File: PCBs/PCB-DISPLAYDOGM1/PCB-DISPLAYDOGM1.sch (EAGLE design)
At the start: 36 parts, among them IC1 MCP23017SS, IC2 74HC14D, SW1 EC12E_SW, SW2 EC12E_SW, SW2ALT EC12E_SW

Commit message: PCBS updated
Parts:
- removed C3: 10uF, SparkFun:CAP0805
- added C10, C12: 100nF, SparkFun:CAP0603-CAP
- added C2: 22uF, SparkFun:CAP0805
- added L4: ILHB0805ER121V, SparkFun:INDUCTOR0805
- C4, C7: value 100nF -> 10nF
- R13, R4, R7: value 10K -> 0R
- R5, R6, R8: value 10K -> 100K
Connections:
- new net ARD_5V: C12.1, L4.1, SERIAL.2
- net 5V: now also C10.1, C2.1, L4.2; no longer C3.1, SERIAL.2
- net GND: now also C10.2, C12.2, C2.2; no longer C3.2
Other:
- note added: "74HCT14D"
- note removed: "POWER"
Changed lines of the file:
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@@
 <part name="SERIAL" library="SparkFun" deviceset="M04X2" device=""/>
 <part name="GND5" library="SparkFun" deviceset="GND" device=""/>
-<part name="U$17" library="SparkFun" deviceset="5V" device=""/>
 <part name="U$19" library="SKAARHOJ" deviceset="3BITADDR" device=""/>
 <part name="U$23" library="SKAARHOJ" deviceset="PCA9671" device=""/>
@@
 <part name="R1" library="SparkFun" deviceset="RESISTOR" device="0603-RES" value="30R/0.1W"/>
 <part name="R3" library="SparkFun" deviceset="RESISTOR" device="0603-RES" value="30R/0.1W"/>
-<part name="C3" library="SparkFun" deviceset="CAP" device="0805" value="10uF"/>
-<part name="U$4" library="SparkFun" deviceset="5V" device=""/>
-<part name="GND3" library="SparkFun" deviceset="GND" device=""/>
 <part name="GND2" library="SparkFun" deviceset="GND" device=""/>
 <part name="SW1" library="switch-alps" deviceset="EC12E_SW" device=""/>
-<part name="C4" library="SparkFun" deviceset="CAP" device="0603-CAP" value="100nF"/>
+<part name="C4" library="SparkFun" deviceset="CAP" device="0603-CAP" value="10nF"/>
 <part name="C5" library="SparkFun" deviceset="CAP" device="0603-CAP" value="10nF"/>
 <part name="C6" library="SparkFun" deviceset="CAP" device="0603-CAP" value="10nF"/>
-<part name="R4" library="SparkFun" deviceset="RESISTOR" device="0603-RES" value="10K"/>
+<part name="R4" library="SparkFun" deviceset="RESISTOR" device="0603-RES" value="0R"/>
 <part name="U$7" library="SKAARHOJ" deviceset="GNDPAD" device="6MM" value="GNDPAD6MM"/>
 <part name="U$21" library="SKAARHOJ" deviceset="GNDPAD" device="6MM" value="GNDPAD6MM"/>
 <part name="GND6" library="SparkFun" deviceset="GND" device=""/>
 <part name="SW2" library="switch-alps" deviceset="EC12E_SW" device=""/>
-<part name="C7" library="SparkFun" deviceset="CAP" device="0603-CAP" value="100nF"/>
+<part name="C7" library="SparkFun" deviceset="CAP" device="0603-CAP" value="10nF"/>
 <part name="C8" library="SparkFun" deviceset="CAP" device="0603-CAP" value="10nF"/>
 <part name="C9" library="SparkFun" deviceset="CAP" device="0603-CAP" value="10nF"/>
-<part name="R13" library="SparkFun" deviceset="RESISTOR" device="0603-RES" value="10K"/>
+<part name="R13" library="SparkFun" deviceset="RESISTOR" device="0603-RES" value="0R"/>
 <part name="IC1" library="microchip" deviceset="MCP23017" device="SS">
 <attribute name="MPN" value="MCP23017-E/SS"/>
@@
 <part name="U$15" library="SparkFun" deviceset="5V" device=""/>
 <part name="U$16" library="SparkFun" deviceset="5V" device=""/>
-<part name="R8" library="SparkFun" deviceset="RESISTOR" device="0603-RES" value="10K"/>
+<part name="R8" library="SparkFun" deviceset="RESISTOR" device="0603-RES" value="100K"/>
 <part name="U$18" library="SparkFun" deviceset="5V" device=""/>
 <part name="GND12" library="SparkFun" deviceset="GND" device=""/>
@@
 <part name="GND4" library="supply1" deviceset="GND" device=""/>
 <part name="U$5" library="SparkFun" deviceset="5V" device=""/>
-<part name="R5" library="SparkFun" deviceset="RESISTOR" device="0603-RES" value="10K"/>
-<part name="R6" library="SparkFun" deviceset="RESISTOR" device="0603-RES" value="10K"/>
-<part name="R7" library="SparkFun" deviceset="RESISTOR" device="0603-RES" value="10K"/>
+<part name="R5" library="SparkFun" deviceset="RESISTOR" device="0603-RES" value="100K"/>
+<part name="R6" library="SparkFun" deviceset="RESISTOR" device="0603-RES" value="100K"/>
+<part name="R7" library="SparkFun" deviceset="RESISTOR" device="0603-RES" value="0R"/>
 <part name="SW2ALT" library="switch-alps" deviceset="EC12E_SW" device=""/>
+<part name="L4" library="SparkFun" deviceset="INDUCTOR" device="0805" value="ILHB0805ER121V"/>
+<part name="C2" library="SparkFun" deviceset="CAP" device="0805" value="22uF"/>
+<part name="C10" library="SparkFun" deviceset="CAP" device="0603-CAP" value="100nF"/>
+<part name="C12" library="SparkFun" deviceset="CAP" device="0603-CAP" value="100nF"/>
+<part name="U$24" library="SparkFun" deviceset="5V" device=""/>
 </parts>
 <sheets>
@@
 <text x="121.92" y="-60.96" size="3.81" layer="97">SERIAL</text>
 <text x="129.54" y="-5.08" size="3.81" layer="97">CONFIG</text>
-<text x="190.5" y="-60.96" size="3.81" layer="97">POWER</text>
 <text x="-99.06" y="-205.74" size="1.778" layer="91">ADR=Bxxx</text>
 <text x="-101.6" y="-218.44" size="3.81" layer="97">CONFIG</text>
+<text x="78.74" y="-148.336" size="1.778" layer="91">74HCT14D</text>
+<text x="78.74" y="-222.25" size="1.778" layer="91">74HCT14D</text>
+<text x="-27.686" y="-148.59" size="1.778" layer="91">74HCT14D</text>
 </plain>
 <instances>
 <instance part="SERIAL" gate="G$1" x="137.16" y="-73.66"/>
 <instance part="GND5" gate="1" x="124.46" y="-86.36"/>
-<instance part="U$17" gate="G$1" x="147.32" y="-68.58"/>
 <instance part="U$19" gate="G$1" x="134.62" y="-22.86"/>
 <instance part="U$23" gate="G$1" x="66.04" y="-43.18" rot="R180"/>
@@
 <instance part="R1" gate="G$1" x="-43.18" y="-15.24" rot="R90"/>
 <instance part="R3" gate="G$1" x="-33.02" y="-15.24" rot="R90"/>
-<instance part="C3" gate="G$1" x="195.58" y="-78.74"/>
-<instance part="U$4" gate="G$1" x="195.58" y="-71.12"/>
-<instance part="GND3" gate="1" x="195.58" y="-86.36"/>
 <instance part="GND2" gate="1" x="7.62" y="-198.12"/>
 <instance part="SW1" gate="G$1" x="60.96" y="-157.48" rot="R90"/>
@@
 <instance part="SW2ALT" gate="G$1" x="162.56" y="-127" rot="R90"/>
 <instance part="SW2ALT" gate="G$2" x="160.02" y="-142.24"/>
+<instance part="L4" gate="G$1" x="182.88" y="-68.58" rot="R90"/>
+<instance part="C2" gate="G$1" x="205.74" y="-76.2"/>
+<instance part="C10" gate="G$1" x="193.04" y="-76.2"/>
+<instance part="C12" gate="G$1" x="172.72" y="-76.2"/>
+<instance part="U$24" gate="G$1" x="205.74" y="-66.04"/>
 </instances>
 <busses>
@@
 <nets>
 <net name="5V" class="1">
-<segment>
-<pinref part="SERIAL" gate="G$1" pin="2"/>
-<pinref part="U$17" gate="G$1" pin="5V"/>
-<wire x1="144.78" y1="-68.58" x2="147.32" y2="-68.58" width="0.1524" layer="91"/>
-</segment>
 <segment>
 <pinref part="R2" gate="G$1" pin="2"/>
@@
 </segment>
 <segment>
-<pinref part="U$4" gate="G$1" pin="5V"/>
-<pinref part="C3" gate="G$1" pin="1"/>
-<wire x1="195.58" y1="-73.66" x2="195.58" y2="-71.12" width="0.1524" layer="91"/>
-</segment>
-<segment>
 <pinref part="IC1" gate="G$1" pin="VDD"/>
 <pinref part="U$13" gate="G$1" pin="5V"/>
@@
 <pinref part="U$5" gate="G$1" pin="5V"/>
 </segment>
+<segment>
+<wire x1="190.5" y1="-68.58" x2="193.04" y2="-68.58" width="0.1524" layer="91"/>
+<pinref part="C10" gate="G$1" pin="1"/>
+<wire x1="193.04" y1="-71.12" x2="193.04" y2="-68.58" width="0.1524" layer="91"/>
+<pinref part="L4" gate="G$1" pin="2"/>
+<pinref part="C2" gate="G$1" pin="1"/>
+<wire x1="205.74" y1="-71.12" x2="205.74" y2="-68.58" width="0.1524" layer="91"/>
+<wire x1="205.74" y1="-68.58" x2="193.04" y2="-68.58" width="0.1524" layer="91"/>
+<junction x="193.04" y="-68.58"/>
+<pinref part="U$24" gate="G$1" pin="5V"/>
+<wire x1="205.74" y1="-66.04" x2="205.74" y2="-68.58" width="0.1524" layer="91"/>
+<junction x="205.74" y="-68.58"/>
+</segment>
 </net>
 <net name="GND" class="1">
@@
 <pinref part="GND5" gate="1" pin="GND"/>
 <wire x1="124.46" y1="-68.58" x2="124.46" y2="-83.82" width="0.1524" layer="91"/>
+<pinref part="C12" gate="G$1" pin="2"/>
+<wire x1="172.72" y1="-83.82" x2="172.72" y2="-78.74" width="0.1524" layer="91"/>
+<pinref part="C10" gate="G$1" pin="2"/>
+<wire x1="172.72" y1="-83.82" x2="193.04" y2="-83.82" width="0.1524" layer="91"/>
+<wire x1="193.04" y1="-83.82" x2="193.04" y2="-78.74" width="0.1524" layer="91"/>
+<pinref part="C2" gate="G$1" pin="2"/>
+<wire x1="193.04" y1="-83.82" x2="205.74" y2="-83.82" width="0.1524" layer="91"/>
+<wire x1="205.74" y1="-83.82" x2="205.74" y2="-78.74" width="0.1524" layer="91"/>
+<junction x="193.04" y="-83.82"/>
+<wire x1="172.72" y1="-83.82" x2="124.46" y2="-83.82" width="0.1524" layer="91"/>
+<junction x="172.72" y="-83.82"/>
+<junction x="124.46" y="-83.82"/>
 </segment>
 <segment>
@@
 <junction x="-35.56" y="-33.02"/>
 <label x="-30.48" y="-33.02" size="1.778" layer="95"/>
-</segment>
-<segment>
-<pinref part="GND3" gate="1" pin="GND"/>
-<pinref part="C3" gate="G$1" pin="2"/>
-<wire x1="195.58" y1="-83.82" x2="195.58" y2="-81.28" width="0.1524" layer="91"/>
 </segment>
 <segment>
@@
 <wire x1="-7.62" y1="-228.6" x2="-7.62" y2="-193.04" width="0.1524" layer="91"/>
 <junction x="-7.62" y="-193.04"/>
+<junction x="-22.86" y="-271.78"/>
 </segment>
 <segment>
@@
 </segment>
 </net>
+<net name="ARD_5V" class="1">
+<segment>
+<pinref part="L4" gate="G$1" pin="1"/>
+<pinref part="C12" gate="G$1" pin="1"/>
+<wire x1="172.72" y1="-68.58" x2="175.26" y2="-68.58" width="0.1524" layer="91"/>
+<wire x1="172.72" y1="-68.58" x2="172.72" y2="-71.12" width="0.1524" layer="91"/>
+<pinref part="SERIAL" gate="G$1" pin="2"/>
+<wire x1="172.72" y1="-68.58" x2="144.78" y2="-68.58" width="0.1524" layer="91"/>
+<junction x="172.72" y="-68.58"/>
+</segment>
+</net>

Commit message: asfd
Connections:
- new net N$7: IC2E.O, IC2F.I
- new net N$8: IC2E.I, SERIAL.7
- net GND: no longer IC2E.I, IC2F.I
- net SPI_SCLK: now also IC2F.O; no longer SERIAL.7
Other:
- moved on the sheet: IC2E, IC2F
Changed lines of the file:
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@@
 <instance part="U$5" gate="G$1" x="200.66" y="-160.02"/>
 <instance part="IC2" gate="B" x="-12.7" y="-251.46"/>
-<instance part="IC2" gate="E" x="-10.16" y="-271.78"/>
-<instance part="IC2" gate="F" x="-10.16" y="-287.02"/>
+<instance part="IC2" gate="E" x="121.92" y="-101.6"/>
+<instance part="IC2" gate="F" x="144.78" y="-101.6"/>
 <instance part="R5" gate="G$1" x="30.48" y="-149.86" rot="R90"/>
 <instance part="R6" gate="G$1" x="134.62" y="-149.86" rot="R90"/>
@@
 <pinref part="IC2" gate="B" pin="I"/>
 <wire x1="-22.86" y1="-251.46" x2="-22.86" y2="-254" width="0.1524" layer="91"/>
-<pinref part="IC2" gate="E" pin="I"/>
-<wire x1="-22.86" y1="-254" x2="-22.86" y2="-271.78" width="0.1524" layer="91"/>
-<wire x1="-22.86" y1="-271.78" x2="-20.32" y2="-271.78" width="0.1524" layer="91"/>
-<wire x1="-22.86" y1="-271.78" x2="-22.86" y2="-289.56" width="0.1524" layer="91"/>
-<pinref part="IC2" gate="F" pin="I"/>
-<wire x1="-22.86" y1="-289.56" x2="-20.32" y2="-289.56" width="0.1524" layer="91"/>
-<wire x1="-20.32" y1="-289.56" x2="-20.32" y2="-287.02" width="0.1524" layer="91"/>
 <wire x1="-22.86" y1="-254" x2="-30.48" y2="-254" width="0.1524" layer="91"/>
 <wire x1="-30.48" y1="-254" x2="-30.48" y2="-228.6" width="0.1524" layer="91"/>
-<junction x="-22.86" y="-254"/>
 <wire x1="-30.48" y1="-228.6" x2="-7.62" y2="-228.6" width="0.1524" layer="91"/>
 <wire x1="-7.62" y1="-228.6" x2="-7.62" y2="-193.04" width="0.1524" layer="91"/>
 <junction x="-7.62" y="-193.04"/>
-<junction x="-22.86" y="-271.78"/>
 </segment>
 <segment>
@@
 <net name="SPI_SCLK" class="0">
 <segment>
-<pinref part="SERIAL" gate="G$1" pin="7"/>
-<wire x1="129.54" y1="-76.2" x2="119.38" y2="-76.2" width="0.1524" layer="91"/>
-<label x="119.38" y="-76.2" size="1.778" layer="95" rot="R180"/>
-</segment>
-<segment>
 <pinref part="DISP" gate="G$1" pin="D6"/>
 <wire x1="-50.8" y1="-68.58" x2="-50.8" y2="-73.66" width="0.1524" layer="91"/>
 <label x="-50.8" y="-73.66" size="1.778" layer="95" rot="R270"/>
+</segment>
+<segment>
+<pinref part="IC2" gate="F" pin="O"/>
+<wire x1="154.94" y1="-101.6" x2="160.02" y2="-101.6" width="0.1524" layer="91"/>
+<label x="160.02" y="-101.6" size="1.778" layer="95"/>
 </segment>
 </net>
@@
 </segment>
 </net>
+<net name="N$7" class="0">
+<segment>
+<pinref part="IC2" gate="E" pin="O"/>
+<pinref part="IC2" gate="F" pin="I"/>
+<wire x1="134.62" y1="-101.6" x2="132.08" y2="-101.6" width="0.1524" layer="91"/>
+</segment>
+</net>
+<net name="N$8" class="0">
+<segment>
+<pinref part="SERIAL" gate="G$1" pin="7"/>
+<wire x1="129.54" y1="-76.2" x2="109.22" y2="-76.2" width="0.1524" layer="91"/>
+<wire x1="109.22" y1="-76.2" x2="109.22" y2="-101.6" width="0.1524" layer="91"/>
+<pinref part="IC2" gate="E" pin="I"/>
+<wire x1="109.22" y1="-101.6" x2="111.76" y2="-101.6" width="0.1524" layer="91"/>
+</segment>
+</net>

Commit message: Updates
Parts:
- SERIAL: value M04X2 -> M04X2M2X4SMALLER; device SparkFun:M04X2 -> SKAARHOJ:M04X2M2X4SMALLER
- U$10, U$19: value 3BITADDR -> 3BITADDRSMALL; device SKAARHOJ:3BITADDR -> SKAARHOJ:3BITADDRSMALL

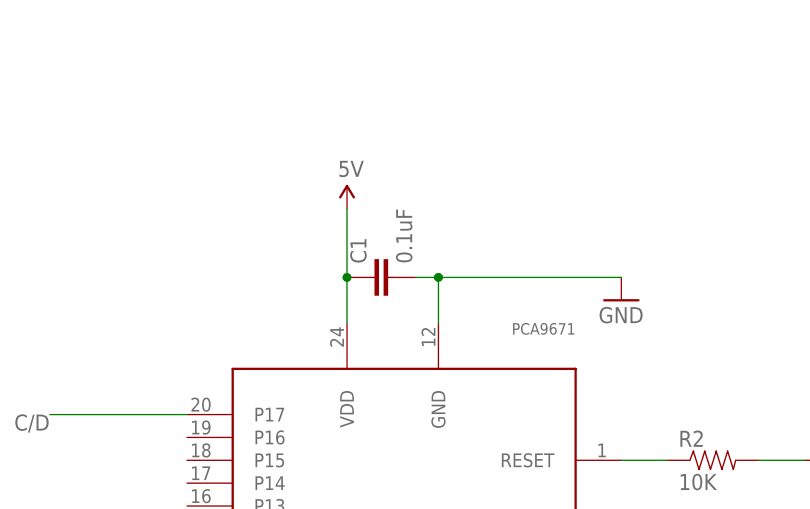
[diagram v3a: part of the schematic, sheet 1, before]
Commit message: Added SKAARHOJ_ID to a lot of PCBs...
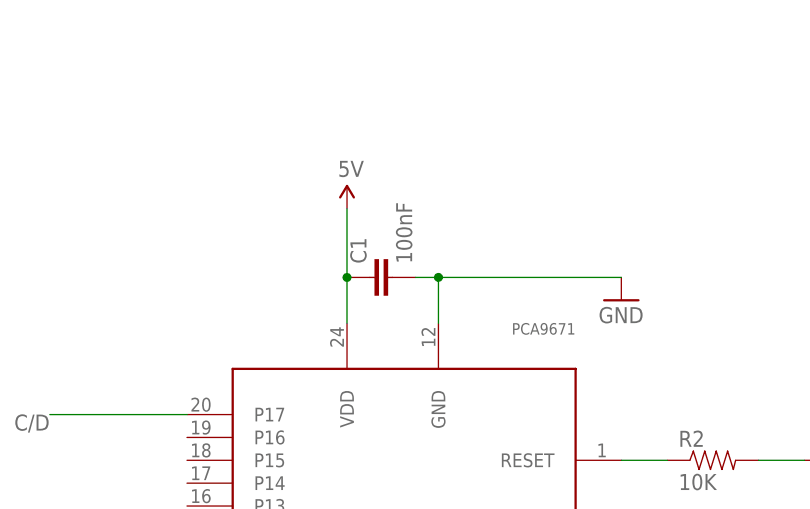
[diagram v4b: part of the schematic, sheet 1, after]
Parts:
- C1: value 0.1uF -> 100nF
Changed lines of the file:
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@@
 <?xml version="1.0" encoding="utf-8"?>
 <!DOCTYPE eagle SYSTEM "eagle.dtd">
-<eagle version="7.5.0">
+<eagle version="7.7.0">
 <drawing>
 <settings>
@@
 <grid distance="0.1" unitdist="inch" unit="inch" style="lines" multiple="1" display="no" altdistance="0.01" altunitdist="inch" altunit="inch"/>
 <layers>
-<layer number="1" name="Top" color="4" fill="1" visible="yes" active="no"/>
-<layer number="2" name="Route2" color="1" fill="3" visible="yes" active="no"/>
-<layer number="3" name="Route3" color="4" fill="3" visible="yes" active="no"/>
-<layer number="4" name="Route4" color="1" fill="4" visible="yes" active="no"/>
-<layer number="5" name="Route5" color="4" fill="4" visible="yes" active="no"/>
-<layer number="6" name="Route6" color="1" fill="8" visible="yes" active="no"/>
-<layer number="7" name="Route7" color="4" fill="8" visible="yes" active="no"/>
-<layer number="8" name="Route8" color="1" fill="2" visible="yes" active="no"/>
-<layer number="9" name="Route9" color="4" fill="2" visible="yes" active="no"/>
-<layer number="10" name="Route10" color="1" fill="7" visible="yes" active="no"/>
-<layer number="11" name="Route11" color="4" fill="7" visible="yes" active="no"/>
-<layer number="12" name="Route12" color="1" fill="5" visible="yes" active="no"/>
-<layer number="13" name="Route13" color="4" fill="5" visible="yes" active="no"/>
-<layer number="14" name="Route14" color="1" fill="6" visible="yes" active="no"/>
-<layer number="15" name="Route15" color="4" fill="6" visible="yes" active="no"/>
-<layer number="16" name="Bottom" color="1" fill="1" visible="yes" active="no"/>
-<layer number="17" name="Pads" color="2" fill="1" visible="yes" active="no"/>
-<layer number="18" name="Vias" color="2" fill="1" visible="yes" active="no"/>
-<layer number="19" name="Unrouted" color="13" fill="1" visible="yes" active="no"/>
-<layer number="20" name="Dimension" color="15" fill="1" visible="yes" active="no"/>
-<layer number="21" name="tPlace" color="7" fill="1" visible="yes" active="no"/>
-<layer number="22" name="bPlace" color="7" fill="1" visible="yes" active="no"/>
-<layer number="23" name="tOrigins" color="15" fill="1" visible="yes" active="no"/>
-<layer number="24" name="bOrigins" color="15" fill="1" visible="yes" active="no"/>
-<layer number="25" name="tNames" color="7" fill="1" visible="yes" active="no"/>
-<layer number="26" name="bNames" color="7" fill="1" visible="yes" active="no"/>
-<layer number="27" name="tValues" color="7" fill="1" visible="yes" active="no"/>
-<layer number="28" name="bValues" color="7" fill="1" visible="yes" active="no"/>
+<layer number="1" name="Top" color="4" fill="1" visible="no" active="no"/>
+<layer number="2" name="Route2" color="1" fill="3" visible="no" active="no"/>
+<layer number="3" name="Route3" color="4" fill="3" visible="no" active="no"/>
+<layer number="4" name="Route4" color="1" fill="4" visible="no" active="no"/>
+<layer number="5" name="Route5" color="4" fill="4" visible="no" active="no"/>
+<layer number="6" name="Route6" color="1" fill="8" visible="no" active="no"/>
+<layer number="7" name="Route7" color="4" fill="8" visible="no" active="no"/>
+<layer number="8" name="Route8" color="1" fill="2" visible="no" active="no"/>
+<layer number="9" name="Route9" color="4" fill="2" visible="no" active="no"/>
+<layer number="10" name="Route10" color="1" fill="7" visible="no" active="no"/>
+<layer number="11" name="Route11" color="4" fill="7" visible="no" active="no"/>
+<layer number="12" name="Route12" color="1" fill="5" visible="no" active="no"/>
+<layer number="13" name="Route13" color="4" fill="5" visible="no" active="no"/>
+<layer number="14" name="Route14" color="1" fill="6" visible="no" active="no"/>
+<layer number="15" name="Route15" color="4" fill="6" visible="no" active="no"/>
+<layer number="16" name="Bottom" color="1" fill="1" visible="no" active="no"/>
+<layer number="17" name="Pads" color="2" fill="1" visible="no" active="no"/>
+<layer number="18" name="Vias" color="2" fill="1" visible="no" active="no"/>
+<layer number="19" name="Unrouted" color="13" fill="1" visible="no" active="no"/>
+<layer number="20" name="Dimension" color="15" fill="1" visible="no" active="no"/>
+<layer number="21" name="tPlace" color="7" fill="1" visible="no" active="no"/>
+<layer number="22" name="bPlace" color="7" fill="1" visible="no" active="no"/>
+<layer number="23" name="tOrigins" color="15" fill="1" visible="no" active="no"/>
+<layer number="24" name="bOrigins" color="15" fill="1" visible="no" active="no"/>
+<layer number="25" name="tNames" color="7" fill="1" visible="no" active="no"/>
+<layer number="26" name="bNames" color="7" fill="1" visible="no" active="no"/>
+<layer number="27" name="tValues" color="7" fill="1" visible="no" active="no"/>
+<layer number="28" name="bValues" color="7" fill="1" visible="no" active="no"/>
 <layer number="29" name="tStop" color="7" fill="3" visible="no" active="no"/>
 <layer number="30" name="bStop" color="7" fill="6" visible="no" active="no"/>
@@
 <layer number="35" name="tGlue" color="7" fill="4" visible="no" active="no"/>
 <layer number="36" name="bGlue" color="7" fill="5" visible="no" active="no"/>
-<layer number="37" name="tTest" color="7" fill="1" visible="yes" active="no"/>
-<layer number="38" name="bTest" color="7" fill="1" visible="yes" active="no"/>
+<layer number="37" name="tTest" color="7" fill="1" visible="no" active="no"/>
+<layer number="38" name="bTest" color="7" fill="1" visible="no" active="no"/>
 <layer number="39" name="tKeepout" color="4" fill="11" visible="no" active="no"/>
 <layer number="40" name="bKeepout" color="1" fill="11" visible="no" active="no"/>
@@
 <layer number="44" name="Drills" color="7" fill="1" visible="no" active="no"/>
 <layer number="45" name="Holes" color="7" fill="1" visible="no" active="no"/>
-<layer number="46" name="Milling" color="3" fill="1" visible="yes" active="no"/>
-<layer number="47" name="Measures" color="7" fill="1" visible="yes" active="no"/>
-<layer number="48" name="Document" color="7" fill="1" visible="yes" active="no"/>
-<layer number="49" name="Reference" color="7" fill="1" visible="yes" active="no"/>
-<layer number="50" name="dxf" color="7" fill="1" visible="yes" active="no"/>
-<layer number="51" name="tDocu" color="7" fill="1" visible="yes" active="no"/>
-<layer number="52" name="bDocu" color="7" fill="1" visible="yes" active="no"/>
-<layer number="53" name="tGND_GNDA" color="7" fill="9" visible="yes" active="no"/>
-<layer number="54" name="bGND_GNDA" color="1" fill="9" visible="yes" active="no"/>
-<layer number="56" name="wert" color="7" fill="1" visible="yes" active="no"/>
-<layer number="57" name="tCAD" color="7" fill="1" visible="yes" active="no"/>
+<layer number="46" name="Milling" color="3" fill="1" visible="no" active="no"/>
+<layer number="47" name="Measures" color="7" fill="1" visible="no" active="no"/>
+<layer number="48" name="Document" color="7" fill="1" visible="no" active="no"/>
+<layer number="49" name="Reference" color="7" fill="1" visible="no" active="no"/>
+<layer number="50" name="dxf" color="7" fill="1" visible="no" active="no"/>
+<layer number="51" name="tDocu" color="7" fill="1" visible="no" active="no"/>
+<layer number="52" name="bDocu" color="7" fill="1" visible="no" active="no"/>
+<layer number="53" name="tGND_GNDA" color="7" fill="9" visible="no" active="no"/>
+<layer number="54" name="bGND_GNDA" color="1" fill="9" visible="no" active="no"/>
+<layer number="56" name="wert" color="7" fill="1" visible="no" active="no"/>
+<layer number="57" name="tCAD" color="7" fill="1" visible="no" active="no"/>
 <layer number="90" name="Modules" color="5" fill="1" visible="yes" active="yes"/>
 <layer number="91" name="Nets" color="2" fill="1" visible="yes" active="yes"/>
@@
 <part name="U$6" library="SparkFun" deviceset="5V" device=""/>
 <part name="GND1" library="SparkFun" deviceset="GND" device=""/>
-<part name="C1" library="SparkFun" deviceset="CAP" device="0603-CAP" value="0.1uF"/>
+<part name="C1" library="SparkFun" deviceset="CAP" device="0603-CAP" value="100nF"/>
 <part name="U$2" library="SKAARHOJ" deviceset="GNDPAD" device="6MM" value="GNDPAD6MM"/>
 <part name="U$20" library="SKAARHOJ" deviceset="GNDPAD" device="6MM" value="GNDPAD6MM"/>
